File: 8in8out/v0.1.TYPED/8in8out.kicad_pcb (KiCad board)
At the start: 2 copper layers, 100.1 x 86.4 mm, 63 parts, among them IC1 ATTINY48-A, J1 RJ45, J2 RJ45, J3 CONN_6, K110 T771D10, K120 T771D10, K130 T771D10, K140 T771D10, K150 T771D10, K160 T771D10, K170 T771D10, K180 T771D10, P1 CONN_5, P100 CONN_2, P101 CONN_2, P102 CONN_2, P103 CONN_2, P105 CONN_2, P106 CONN_2, P110 CONN_2, P120 CONN_2, P130 CONN_2, P140 CONN_2, P150 CONN_2, P160 CONN_2, P170 CONN_2, P180 CONN_2, P2 CONN_5, P3 CONN_10X2, P4 CONN_2, U1 7805, U10 OPTO-TRANSISTOR, U2 ULN2803, U20 OPTO-TRANSISTOR, U30 OPTO-TRANSISTOR, U40 OPTO-TRANSISTOR, U50 OPTO-TRANSISTOR, U60 OPTO-TRANSISTOR, U70 OPTO-TRANSISTOR, U80 OPTO-TRANSISTOR

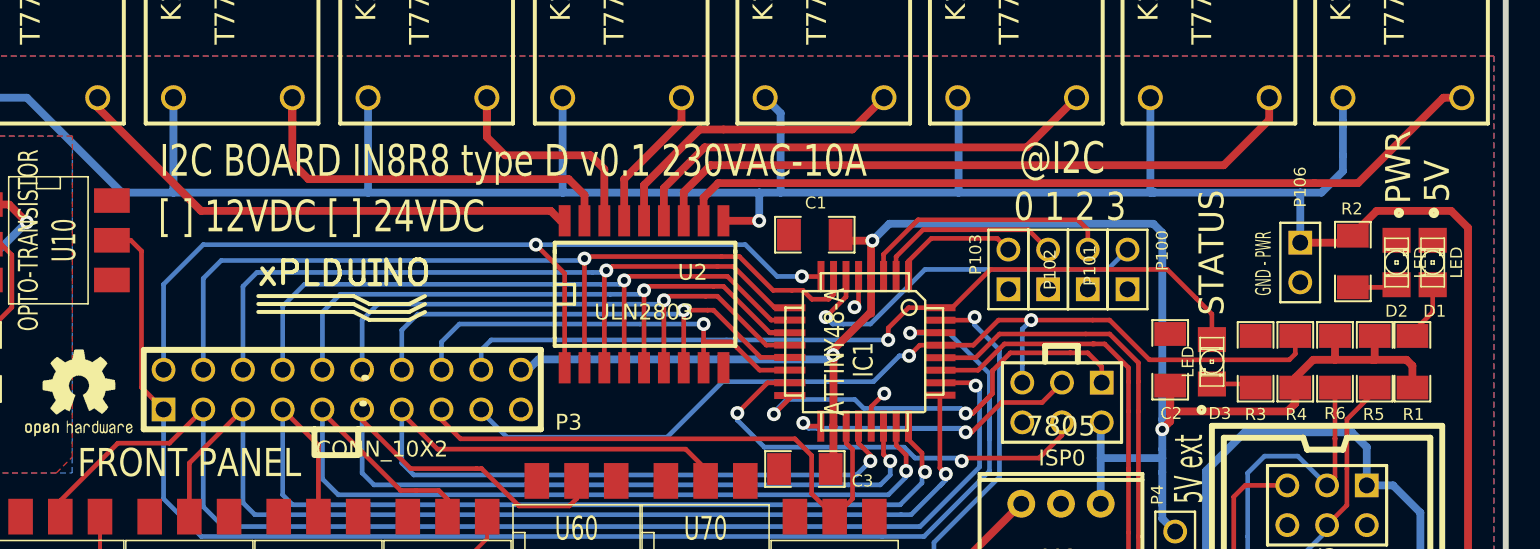
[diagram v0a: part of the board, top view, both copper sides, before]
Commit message: deplacement ULN2803 pour degagement connecteur extension
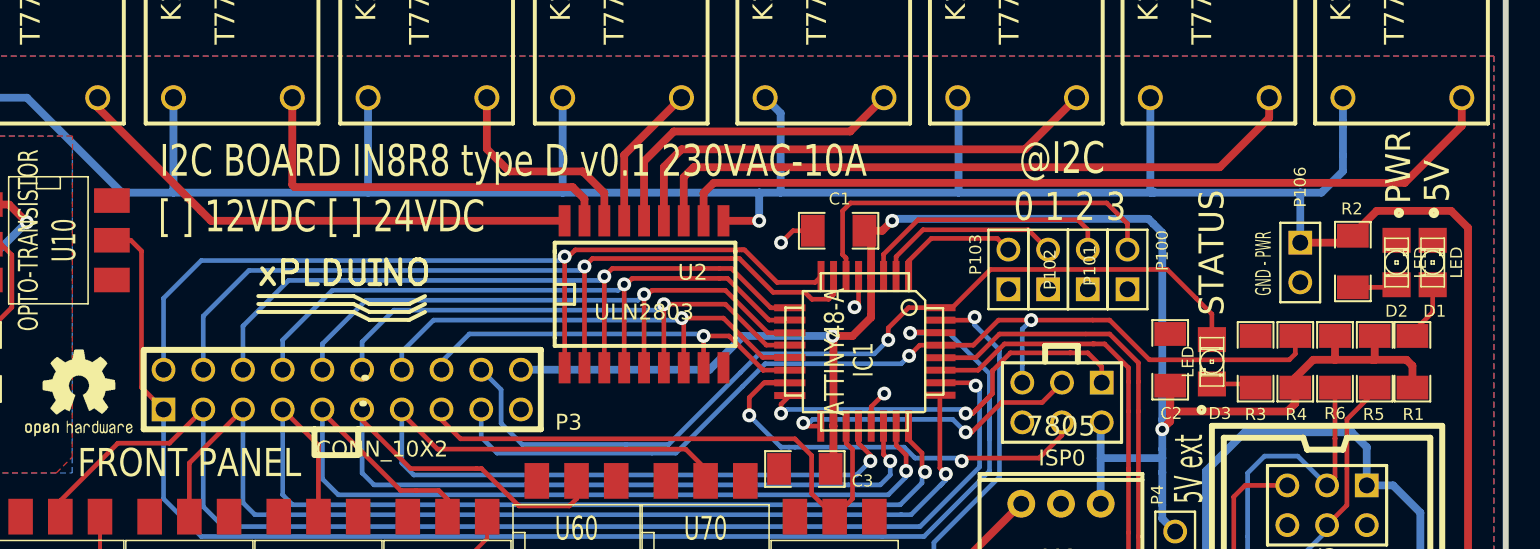
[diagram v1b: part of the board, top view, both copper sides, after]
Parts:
- moved C1 1.55 mm to (239.0, 113.5)
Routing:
- net SCK: track 29.3 -> 20.6 mm
- net LED: track 53.4 -> 57.9 mm
- net OUT4: track 41.7 -> 38.8 mm
- net GND: track 18.9 -> 21.2 mm, vias 5 -> 6
- net R2: track 16.0 -> 13.7 mm
- net OUT1: track 56.2 -> 54.1 mm
- net OUT2: track 48.3 -> 46.3 mm
- net OUT0: track 58.1 -> 56.0 mm, vias 2 -> 1
- net RESET: track 62.6 -> 64.4 mm
- net OUT3: track 44.0 -> 42.4 mm
- net OUT6: track 32.8 -> 31.3 mm
- net OUT7: track 28.2 -> 26.7 mm
- net OUT5: track 36.8 -> 35.3 mm
- net MISO: track 29.1 -> 27.8 mm
- net R7: track 52.6 -> 53.9 mm
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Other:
- board text removed: "DEPLACER ULN"

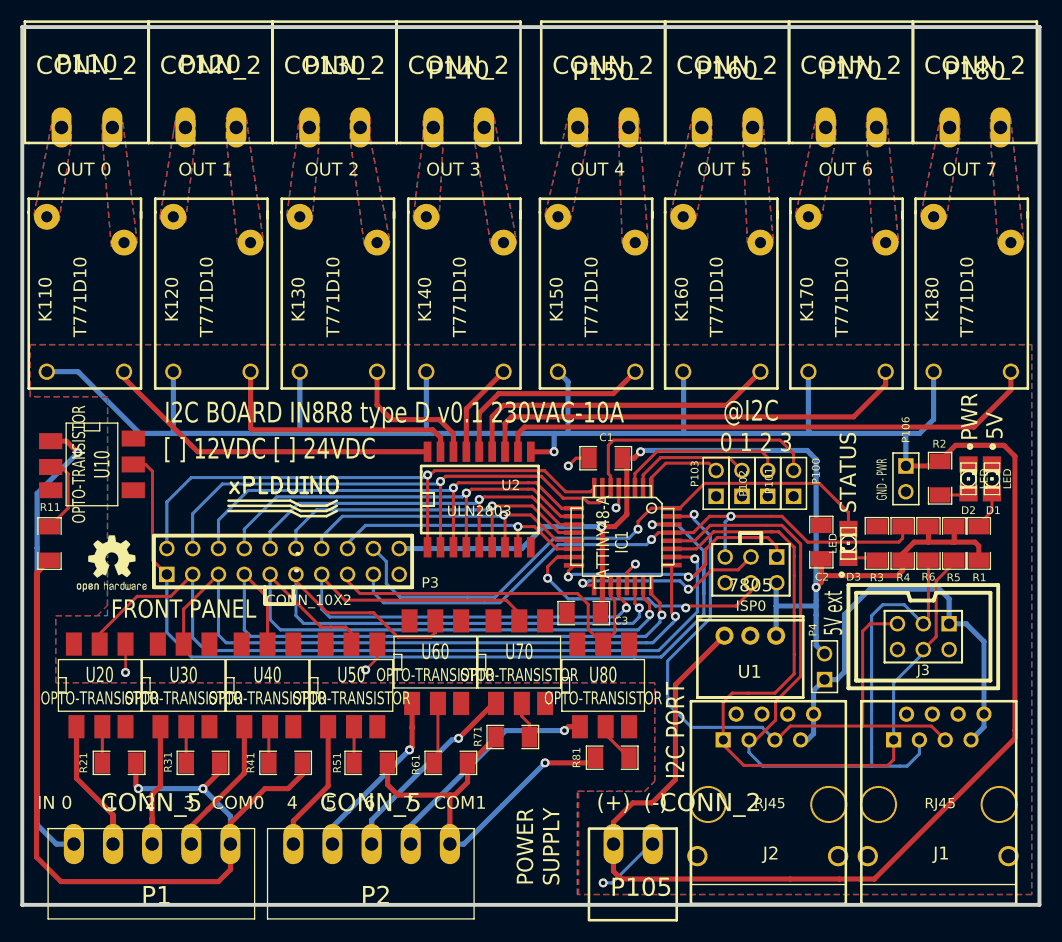
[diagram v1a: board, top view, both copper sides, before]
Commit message: elargissement ecartement pads CMS6 reprise plan de masse
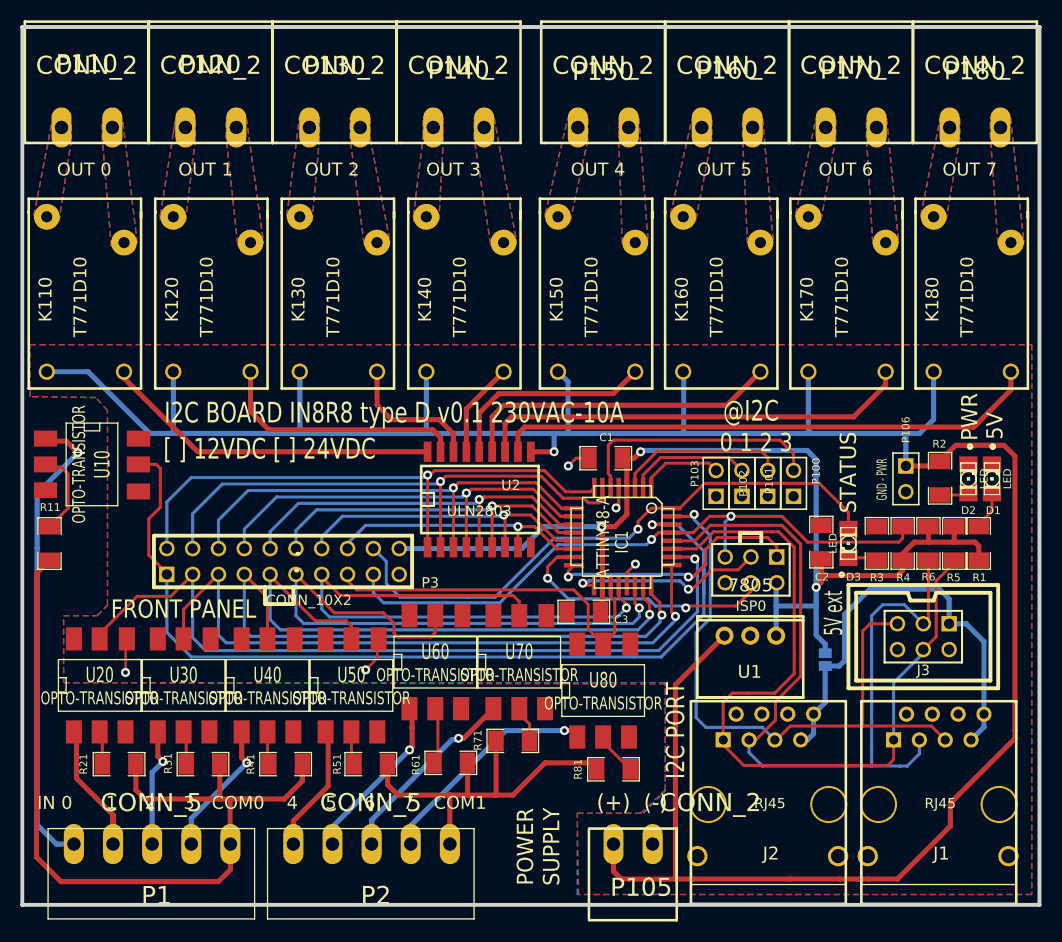
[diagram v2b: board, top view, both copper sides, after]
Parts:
- removed G***: LOGO, OSHWLOGO0.3IN
- removed P4: CONN_2, PIN_ARRAY_2X1
- removed logo_xplduino: VAL**, logo_xplduino
- added GS1: GS2, GS2, B.Cu at (260.6, 133.3)
- moved R81 1.15 mm to (239.8, 144.1)
- moved U80 0.51 mm to (238.8, 136.4)
- moved R71 0.38 mm to (229.9, 141.4)
- moved R21 0.13 mm to (191.1, 143.6)
- moved R31 0.13 mm to (199.4, 143.6)
- moved R41 0.13 mm to (207.5, 143.6)
- moved R51 0.13 mm to (215.9, 143.6)
- moved C3 0.13 mm to (236.9, 128.7)
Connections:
- J1 pad 9: (no net) -> GND
- J2 pad 9: (no net) -> GND
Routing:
- net GND: track 21.2 -> 14.0 mm, vias 6 -> 5
- net /INT: track 66.3 -> 63.2 mm
- net N-0000055: track 7.41 -> 4.28 mm
- net COM1: track 38.6 -> 36.2 mm, vias 1 -> 0
- net CMD5: track 61.8 -> 60.4 mm
- net +12V: track 255.1 -> 256.2 mm
- net IN2: track 12.8 -> 11.7 mm, vias 0 -> 1
- net CMD0: track 94.8 -> 95.9 mm
- net R1: track 26.0 -> 25.1 mm
- net CMD6: track 59.5 -> 58.7 mm
- net N-0000058: track 3.92 -> 3.28 mm
- net IN3: track 13.8 -> 13.5 mm, vias 0 -> 1
- net COM0: track 82.6 -> 82.4 mm, vias 2 -> 0

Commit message: correction table adressage modif uln et routage controle ok, gerber ok, pret pour prod
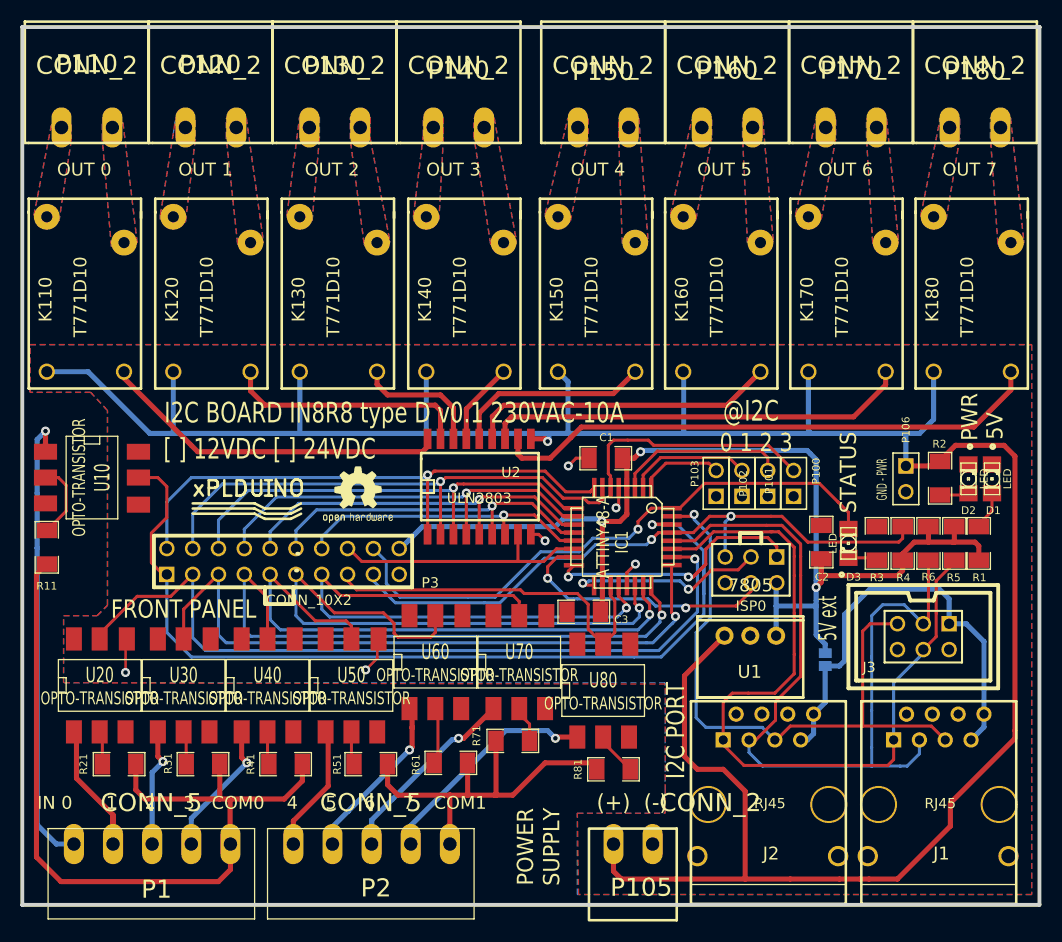
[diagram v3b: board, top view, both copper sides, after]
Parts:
- added G***: LOGO, OSHWLOGO0.3IN, F.Cu at (210.8, 113.4)
- added logo_xplduino: VAL**, logo_xplduino, F.Cu at (203.7, 118.2)
- moved U10 1.30 mm to (188.5, 115.4)
- moved U2 1.27 mm to (226.6, 116.3)
- moved R11 0.45 mm to (184.0, 122.3)
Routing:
- net +12V: track 256.2 -> 258.1 mm
- net GND: track 14.0 -> 15.7 mm, vias 5 -> 6
- net OUT1: track 54.1 -> 52.7 mm
- net OUT4: track 38.8 -> 37.5 mm
- net R4: track 20.8 -> 19.6 mm
- net R3: track 9.39 -> 8.12 mm
- net R6: track 43.1 -> 41.8 mm
- net R5: track 31.7 -> 30.5 mm
- net OUT6: track 31.3 -> 30.2 mm
- net R0: track 33.5 -> 34.5 mm
- net R2: track 13.7 -> 12.8 mm
- net A3: track 24.9 -> 24.0 mm
- net OUT5: track 35.3 -> 34.3 mm
- net R7: track 53.9 -> 54.8 mm
- net R1: track 25.1 -> 24.2 mm
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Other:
- board text added: "3 2 1 0 ID 0 0 0 0 0 0 0 0 1 1 0 0 1 0 2 0 0 1 1 3 0 1 0 0 4 0 1 0 1 5 0 1 1 0 6 0 1 1 1 7 1 0 0 0 8 1 0 0 1 9 1 0 1 0 10 1 0 1 1 11 1 1 0 0 12 1 1 0 1 13 1 1 1 0 14 1 1 1 1 15"
- board text removed: "3 2 1 0 ID 0 0 0 0 0 0 0 0 1 1 0 1 1 0 2 0 1 1 1 3 0 0 0 0 4 0 0 0 1 5 0 1 1 0 6 0 1 1 1 7 1 0 0 0 8 1 0 0 1 9 1 1 1 0 10 1 1 1 1 11 1 0 0 0 12 1 0 0 1 13 1 1 1 0 14 1 1 1 1 15"
